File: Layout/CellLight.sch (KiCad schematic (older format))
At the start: 0 parts

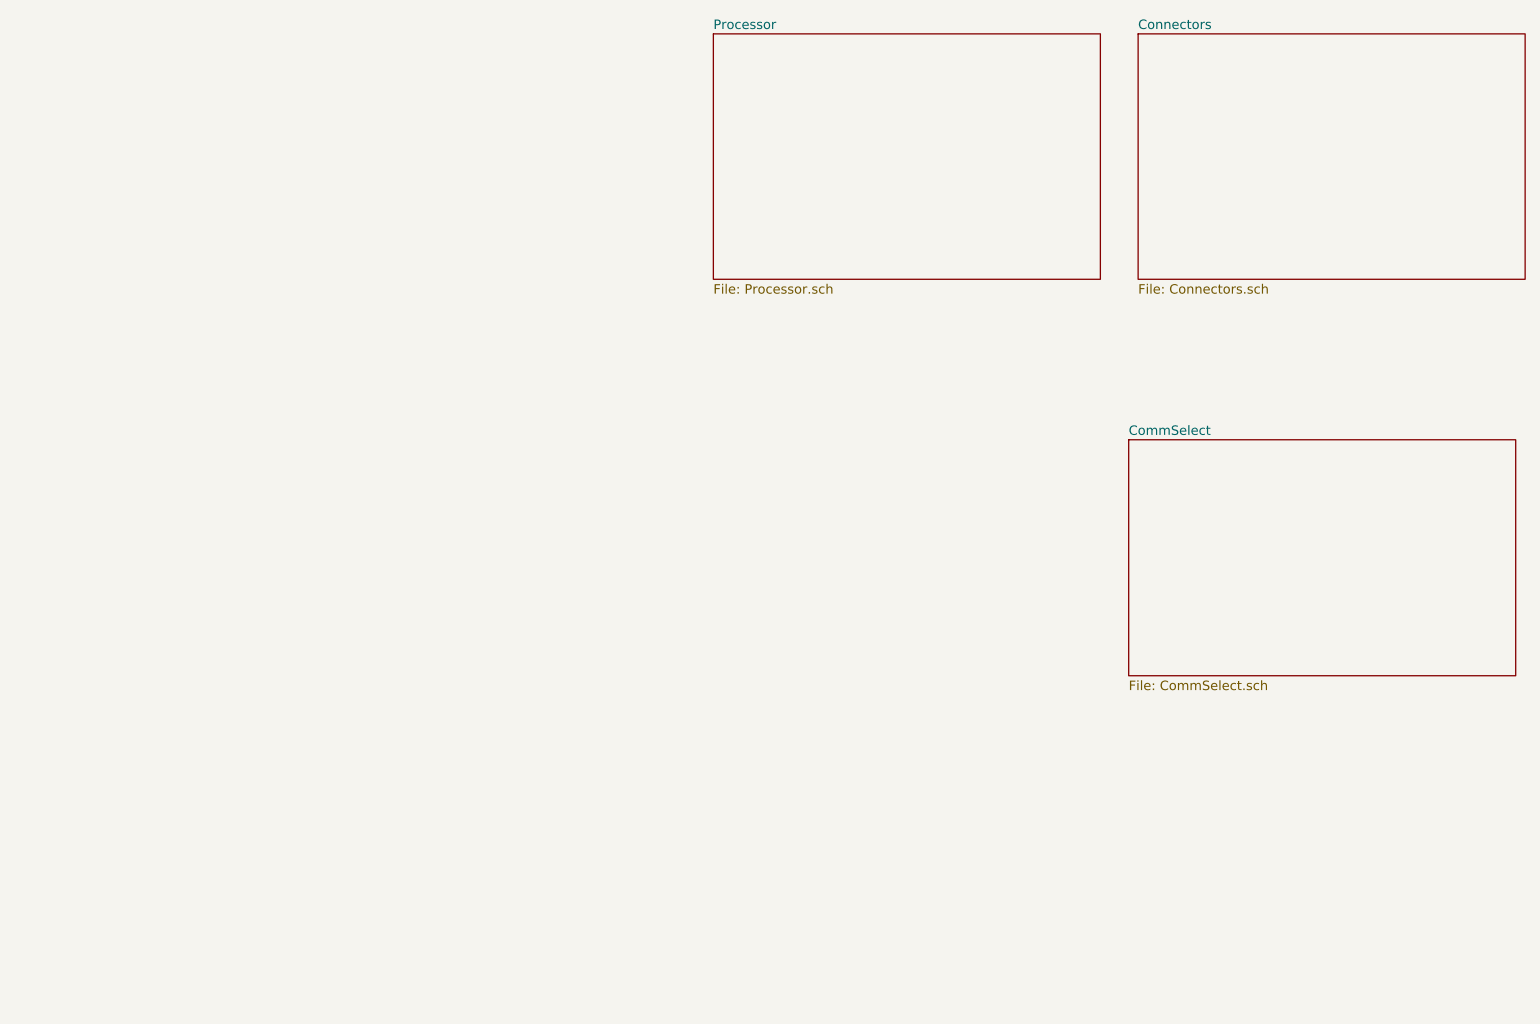
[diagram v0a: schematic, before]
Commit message: Add more sheets. Add LEDs
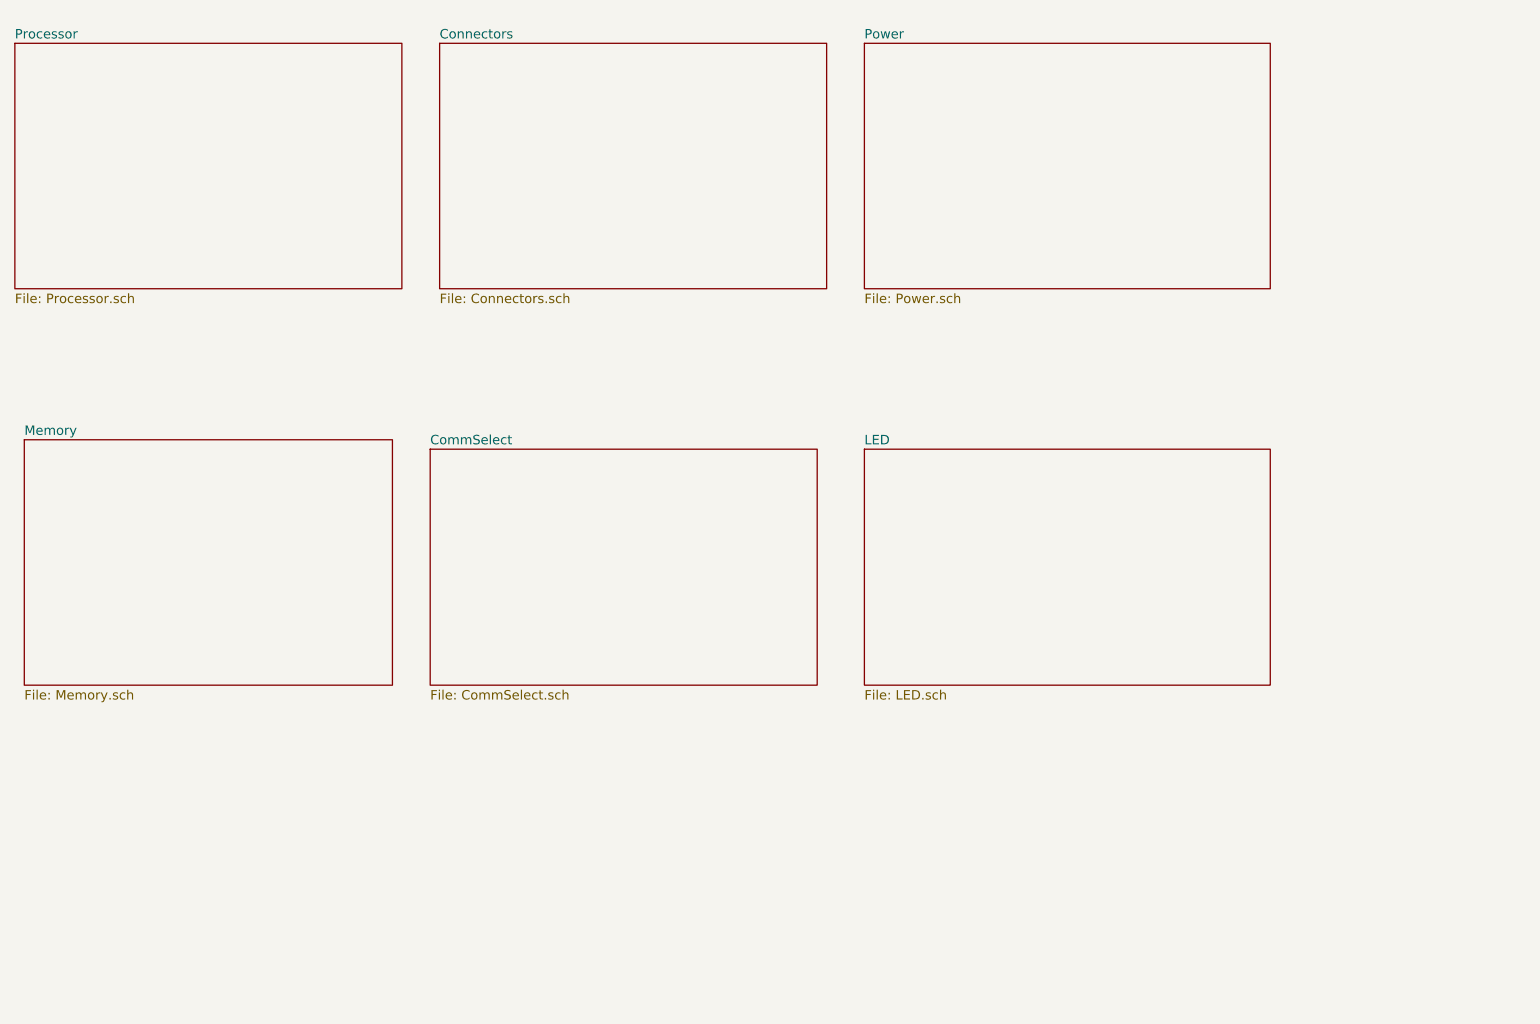
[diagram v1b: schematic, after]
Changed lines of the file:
@@
 $Descr A4 11693 8268
 encoding utf-8
-Sheet 1 4
+Sheet 1 7
 Title ""
 Date ""
@@
 $EndDescr
 $Sheet
-S 5800 1250 2050 1300
+S 2100 1300 2050 1300
 U 5F354543
 F0 "Processor" 50
@@
 $EndSheet
 $Sheet
-S 8050 1250 2050 1300
+S 4350 1300 2050 1300
 U 5F3717FF
 F0 "Connectors" 50
@@
 $EndSheet
 $Sheet
-S 8000 3400 2050 1250
+S 4300 3450 2050 1250
 U 5F373590
 F0 "CommSelect" 50
 F1 "CommSelect.sch" 50
 $EndSheet
+$Sheet
+S 2150 3400 1950 1300
+U 5F395CF0
+F0 "Memory" 50
+F1 "Memory.sch" 50
+$EndSheet
+$Sheet
+S 6600 1300 2150 1300
+U 5F395F1A
+F0 "Power" 50
+F1 "Power.sch" 50
+$EndSheet
+$Sheet
+S 6600 3450 2150 1250
+U 5F3972E9
+F0 "LED" 50
+F1 "LED.sch" 50
+$EndSheet
 $EndSCHEMATC

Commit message: Update schematic for new processor
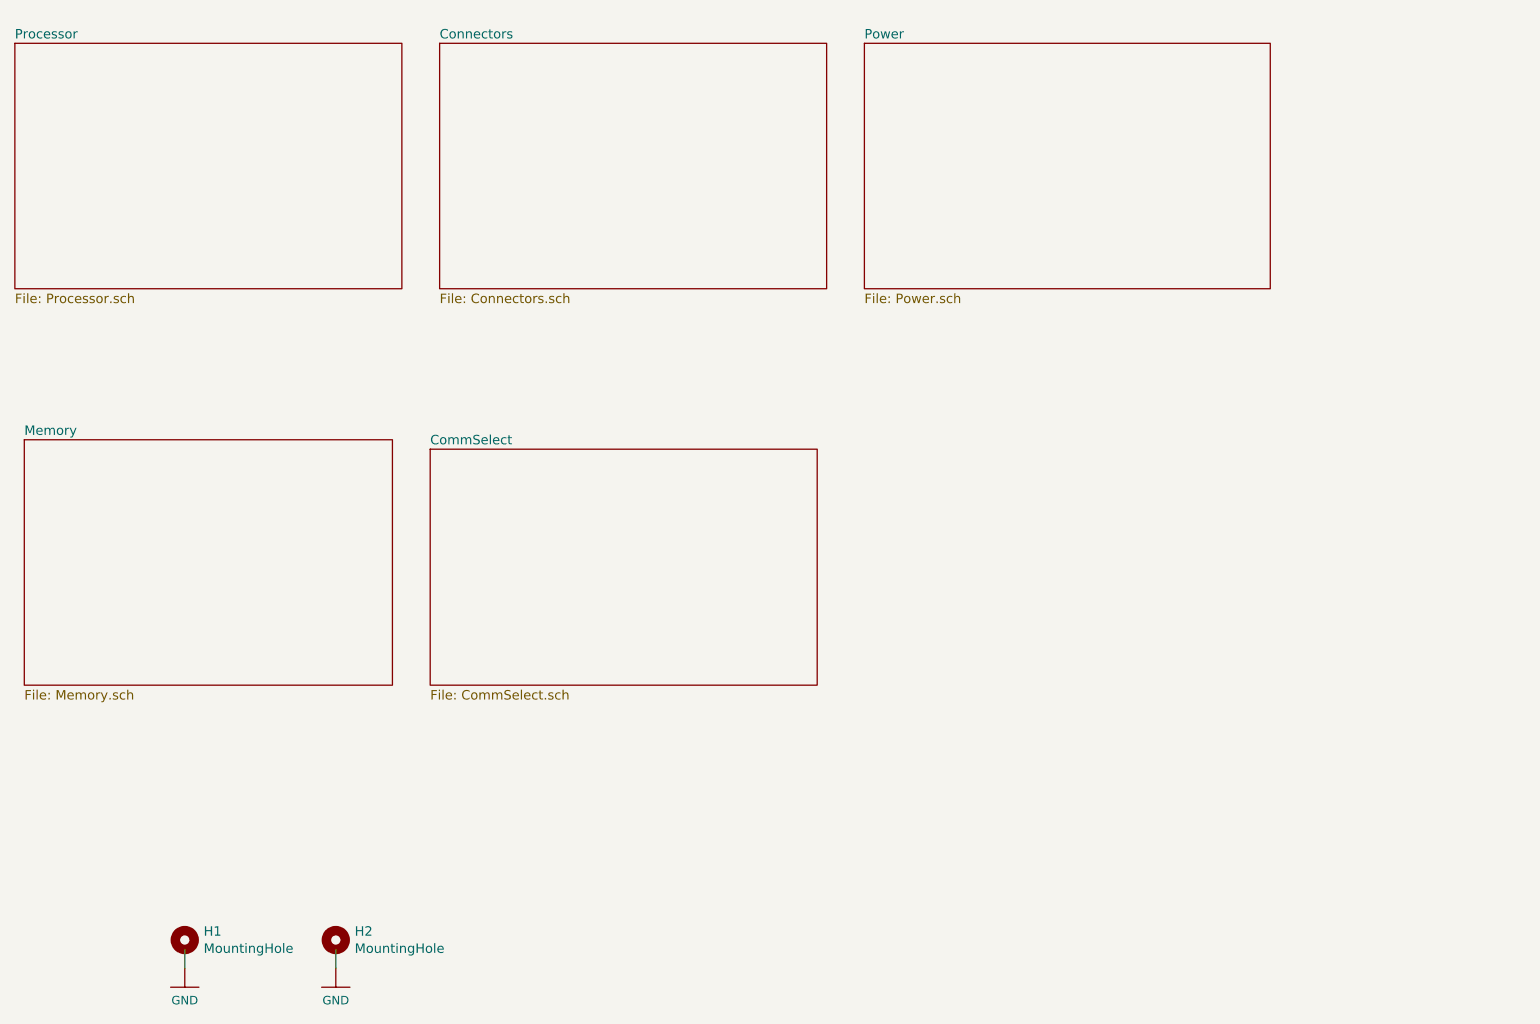
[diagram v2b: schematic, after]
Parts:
- added H1, H2: MountingHole, MountingHole:MountingHole_2.7mm_M2.5_Pad, symbol Mechanical:MountingHole
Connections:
- net labels added: GND
- wire segments 0 -> 2
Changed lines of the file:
@@
 $Descr A4 11693 8268
 encoding utf-8
-Sheet 1 7
+Sheet 1 6
 Title ""
 Date ""
@@
 F1 "Power.sch" 50
 $EndSheet
-$Sheet
-S 6600 3450 2150 1250
-U 5F3972E9
-F0 "LED" 50
-F1 "LED.sch" 50
-$EndSheet
+$Comp
+L Mechanical:MountingHole H1
+U 1 1 5FA88BAA
+P 3000 6050
+F 0 "H1" H 3100 6096 50  0000 L CNN
+F 1 "MountingHole" H 3100 6005 50  0000 L CNN
+F 2 "MountingHole:MountingHole_2.7mm_M2.5_Pad" H 3000 6050 50  0001 C CNN
+F 3 "~" H 3000 6050 50  0001 C CNN
+	1    3000 6050
+	1    0    0    -1
+$EndComp
+$Comp
+L Mechanical:MountingHole H2
+U 1 1 5FA88DD2
+P 3800 6050
+F 0 "H2" H 3900 6096 50  0000 L CNN
+F 1 "MountingHole" H 3900 6005 50  0000 L CNN
+F 2 "MountingHole:MountingHole_2.7mm_M2.5_Pad" H 3800 6050 50  0001 C CNN
+F 3 "~" H 3800 6050 50  0001 C CNN
+	1    3800 6050
+	1    0    0    -1
+$EndComp
+Wire Wire Line
+	3800 6100 3800 6200
+Wire Wire Line
+	3000 6100 3000 6200
+$Comp
+L SparkFun-PowerSymbols:GND #GND0104
+U 1 1 5FA89469
+P 3000 6200
+F 0 "#GND0104" H 3050 6150 45  0001 L BNN
+F 1 "GND" H 3000 6030 45  0000 C CNN
+F 2 "" H 3000 6100 60  0001 C CNN
+F 3 "" H 3000 6100 60  0001 C CNN
+	1    3000 6200
+	1    0    0    -1
+$EndComp
+$Comp
+L SparkFun-PowerSymbols:GND #GND0105
+U 1 1 5FA895DD
+P 3800 6200
+F 0 "#GND0105" H 3850 6150 45  0001 L BNN
+F 1 "GND" H 3800 6030 45  0000 C CNN
+F 2 "" H 3800 6100 60  0001 C CNN
+F 3 "" H 3800 6100 60  0001 C CNN
+	1    3800 6200
+	1    0    0    -1
+$EndComp
 $EndSCHEMATC
